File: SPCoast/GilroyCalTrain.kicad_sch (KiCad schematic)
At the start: 90 parts, among them SW3771 771, SW3773 773, SW3775 775

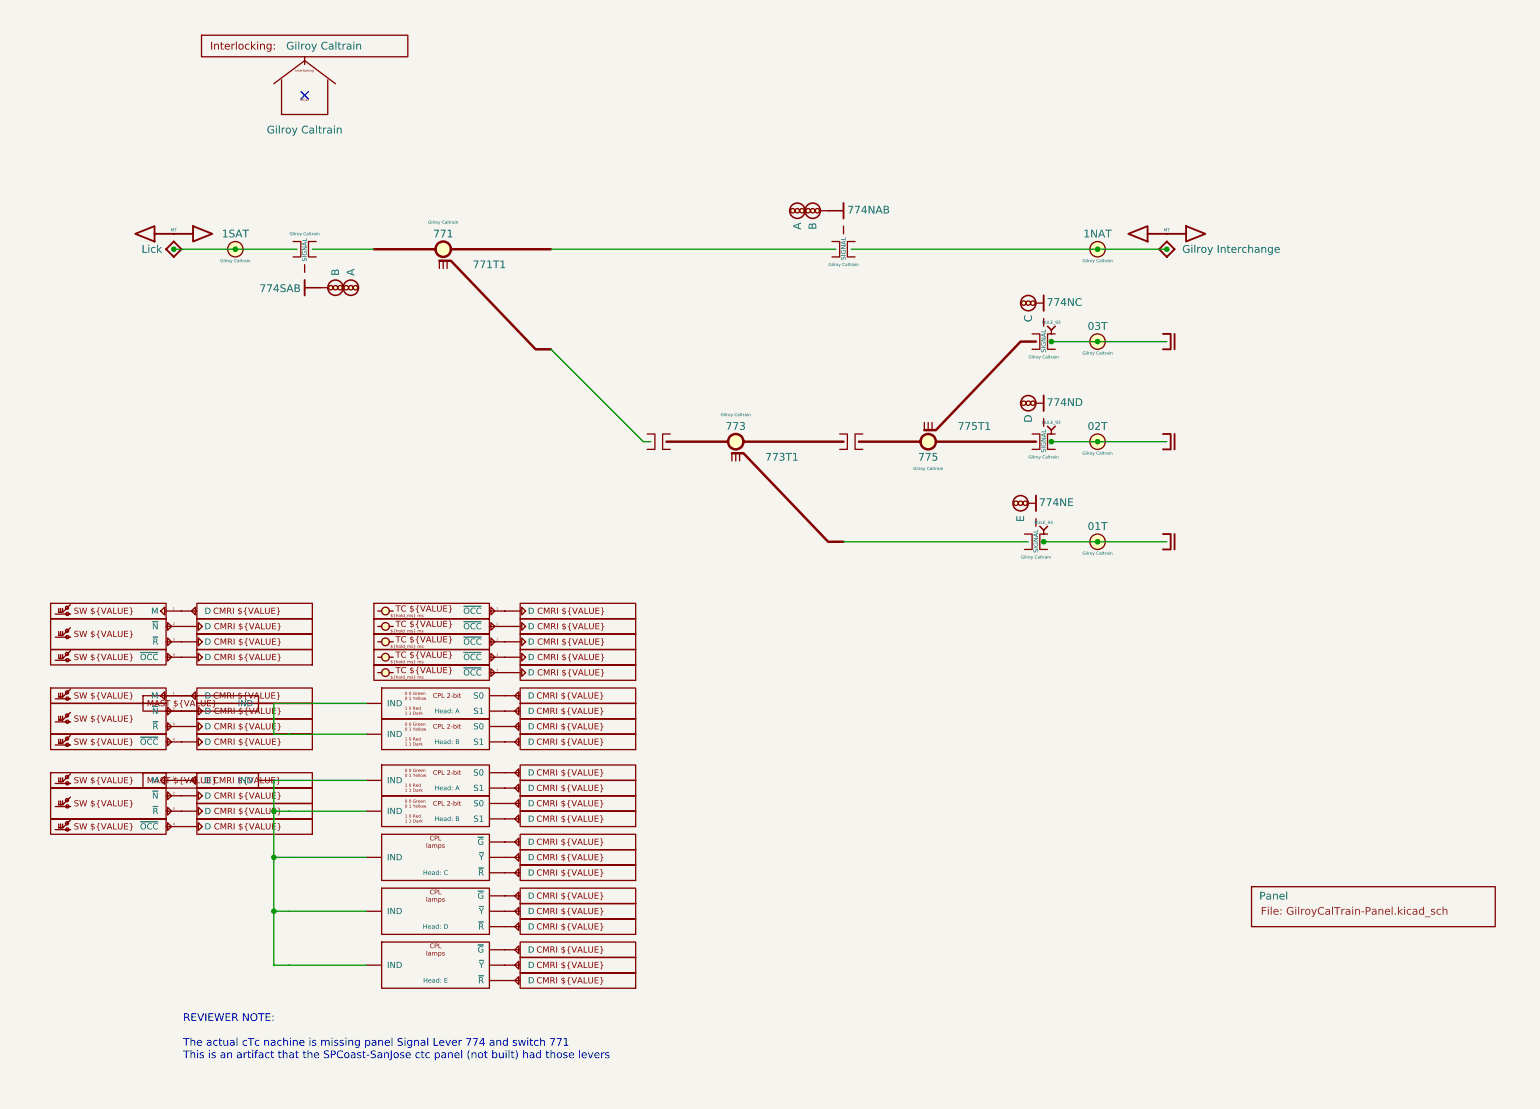
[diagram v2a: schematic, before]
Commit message: refactor(kicad): one Mast per trackplan mast; no library defaults for per-instance facts
Owner's regroup (Sargent, Gilroy Caltrain): the Mast anchors are now the
trackplan masts, Value for Value: 836NAB, 836SA, 836SB, 774NAB, 774SAB,
774NC, 774ND, 774NE. Each head cast hangs on the IND of the mast whose name
lists its letter; 836SB carries its semaphore arm and spectacle RGB as one
Head B. The earlier "836S"/"774N" masts were a lever-direction grouping,
not masts, and are gone. Sargent Exp2 (PCA9685 0x27) channels re-placed by
the owner; the two stray IND stubs on Caltrain removed.

Owner's library tidy: cast bodies one width (-21.59..-2.54), IND pin at
-24.13, Head shown 1.27 left-justified, encoder table outside the body,
Semaphore Style hidden behind "${STYLE} arm".

Library defaults that are per-instance facts are now empty, so KiCad's
field reset can no longer plant plausible wrong values: PanelLamp-*
IndicationToken (was "S"), PanelColumn Interlocking (was "Luchessa"),
Codeline-Encoding-*/Transport-MQTT Station (was "${SHEETNAME}", which
resolves to "Panel"), Interlocking Value (was "${TITLE}"), MCP23017 and
PCA9685 Address (was "0x20"). Mast and Cast-Head-* descriptions follow the
model: Value = the trackplan mast; Head = one of the letters its name lists.

The owner's save had run "Update Symbols from Library" with field reset a
second time; 94 per-instance values (IndicationToken, Interlocking,
Station, Exp2 0x27) restored from the last good netlist by
edits/2026-10-17-restore-reset-fields.py. Its stale CMRI entries wrote bit
numbers into 32 Caltrain CMRI Addresses on the way; put back to 30 and the
entries removed. Sheet lib_symbols caches refreshed (45) to the libraries.

Verified:
- kicad-cli ERC, all severities: 0 violations
- lint_symbol_fields.py: 90 symbols, 0 errors
- sync-library-fields dry run: 0 instances to change
- production/post-head.net vs production/post-restore.net: every mast Value
  is a trackplan mast on its sheet; every cast sits on on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
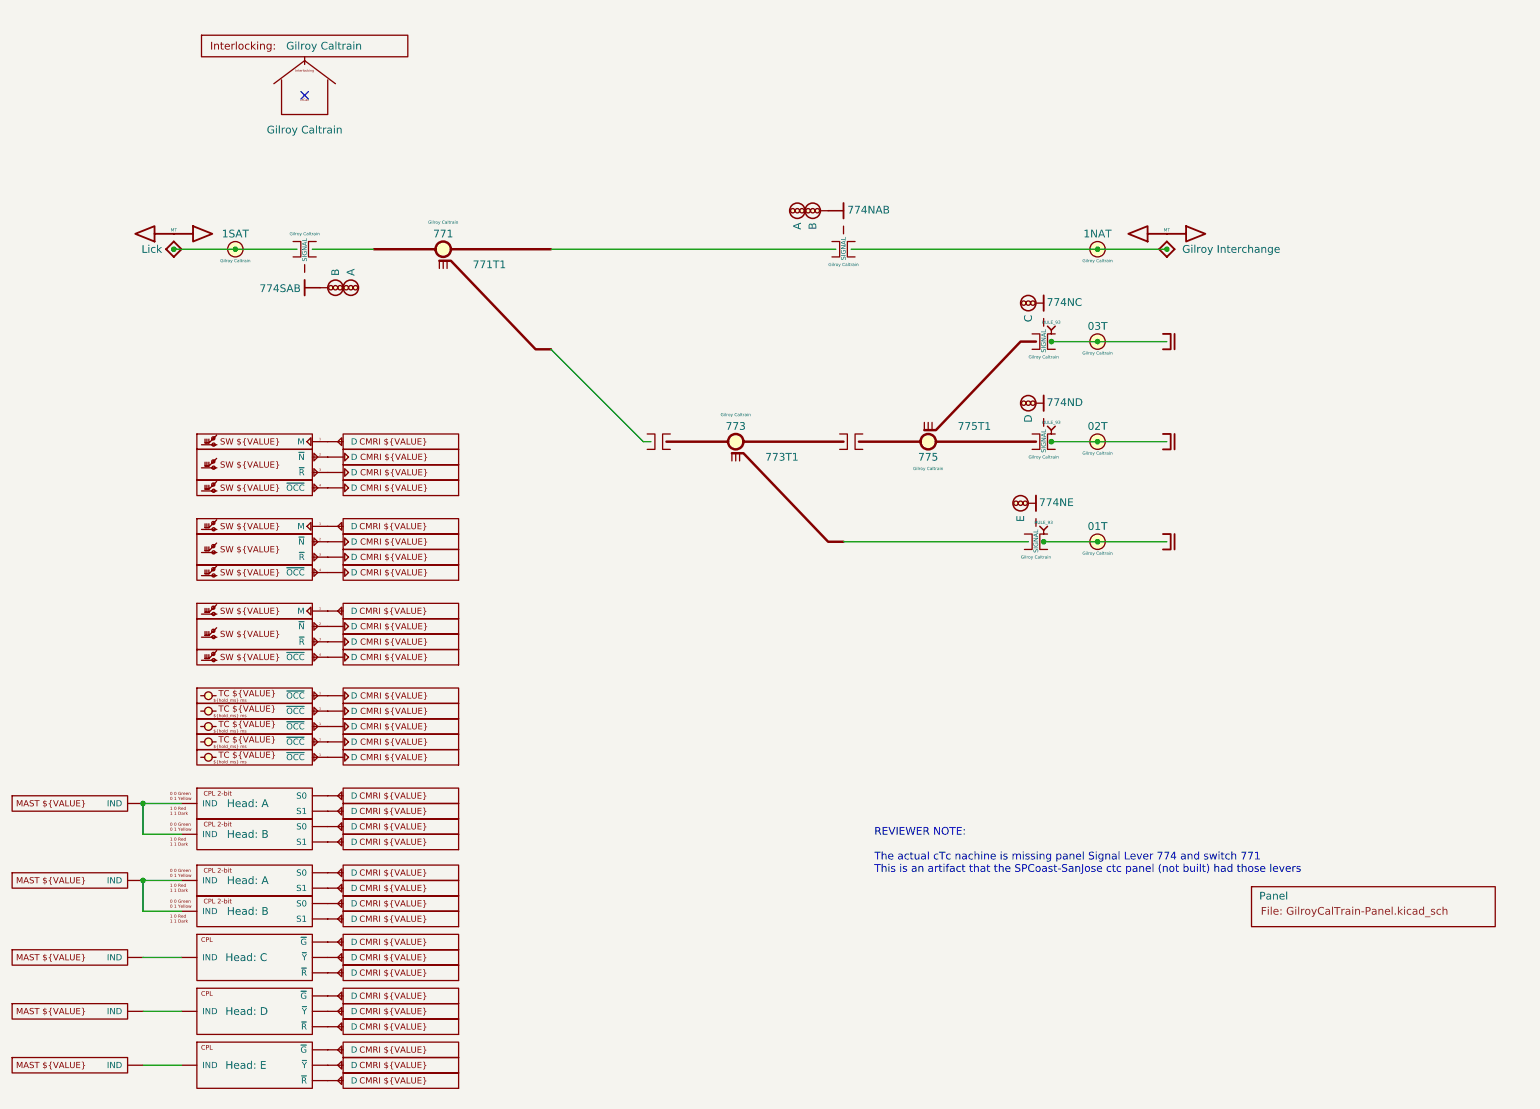
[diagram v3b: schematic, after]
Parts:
- added DevMast5: 774NC, symbol Railroad-Field:Mast
- added DevMast6: 774ND, symbol Railroad-Field:Mast
- added DevMast7: 774NE, symbol Railroad-Field:Mast
- DevMast3: value 774N -> 774NAB
- DevMast4: value 774S -> 774SAB
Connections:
- net at Cast11.3 (IND), Cast8.3 (IND), DevMast3.1 (IND): no longer Cast6.4 (IND), Cast7.4 (IND), Cast9.4 (IND)
- new net: Cast9.4 (IND), DevMast7.1 (IND)
- new net: Cast6.4 (IND), DevMast6.1 (IND)
- new net: Cast7.4 (IND), DevMast5.1 (IND)

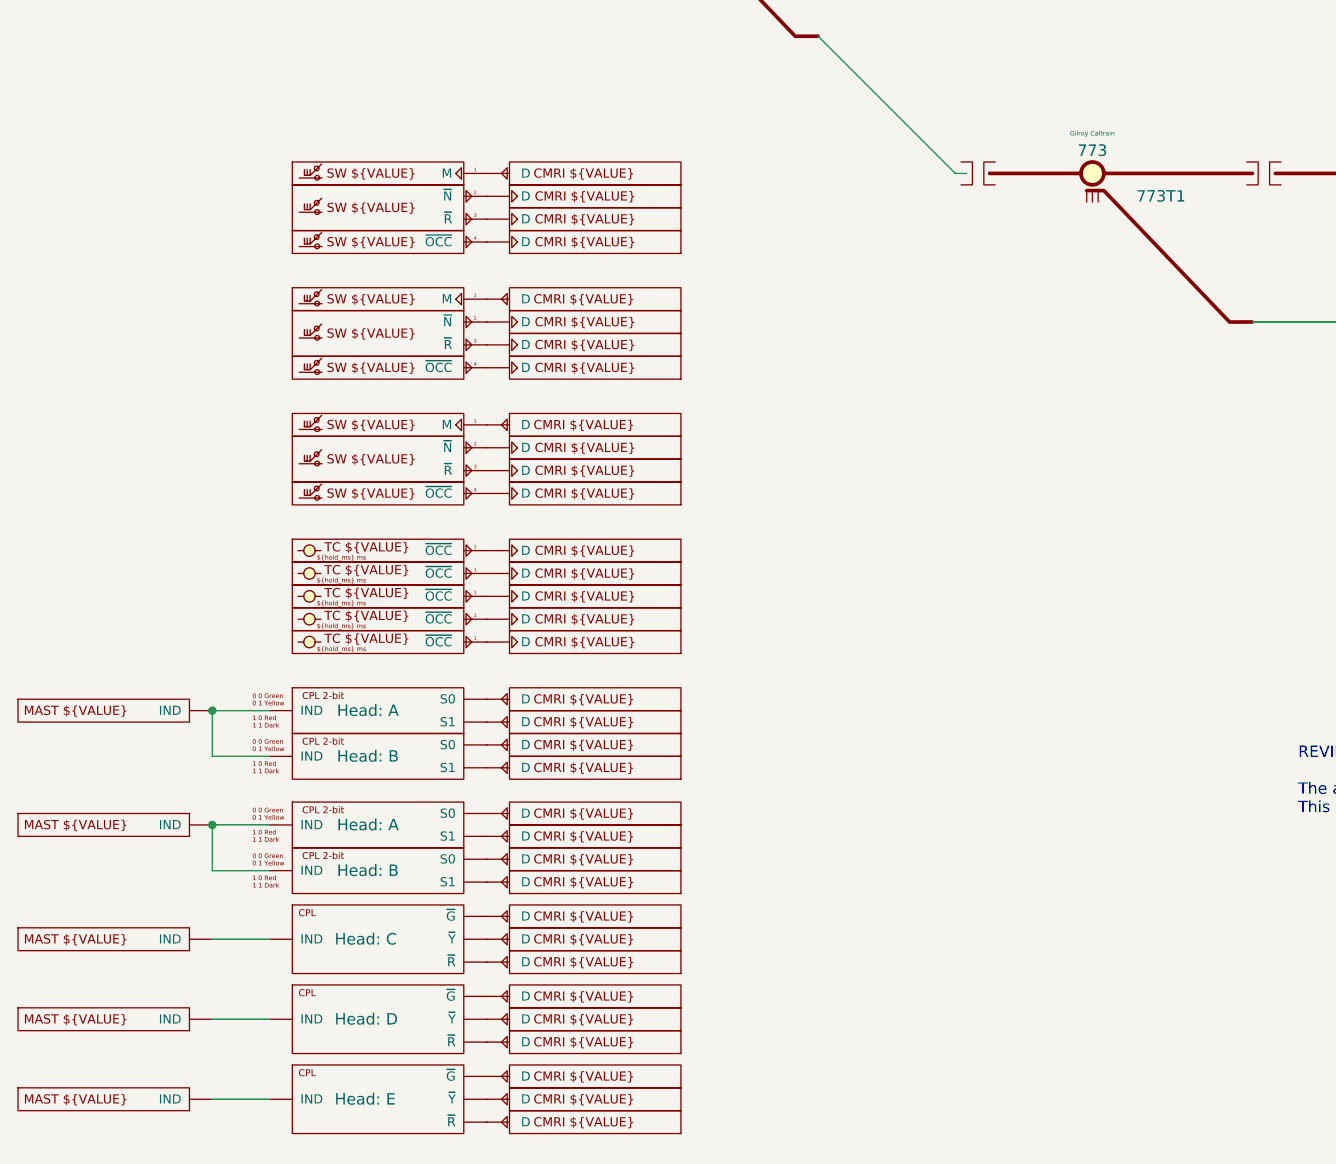
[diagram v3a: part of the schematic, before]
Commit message: chore(kicad): owner edits: GPIO drivers carry Address, Sargent I2C addresses, CMRI body text from fields
Baseline of the owner's saved work before the ADR 0005 scripts:
- Driver-GPIO-Digital and Driver-GPIO-Pixel gain an Address field (the
  board pin); Value renders ${Address}; body text and arrow adjusted.
- Driver-CMRI-IB/OB body text renders UA${Address}.IN/OUT.${Bit} from
  the fields instead of ${VALUE}.
- Sargent, Gilroy Interchange and Luchessa GPIO instances carry Address;
  Sargent Exp2 back at 0x26, Exp3 0x27.
- All sheets resaved by KiCad 10 (reordering), project file
  used_designators cleared by KiCad.

Verified: no lock files; committed as saved, unverified by netlist (the
baseline netlist is exported in the next step).

Co-Authored-By: Claude Fable 5.1 <noreply@anthropic.com>
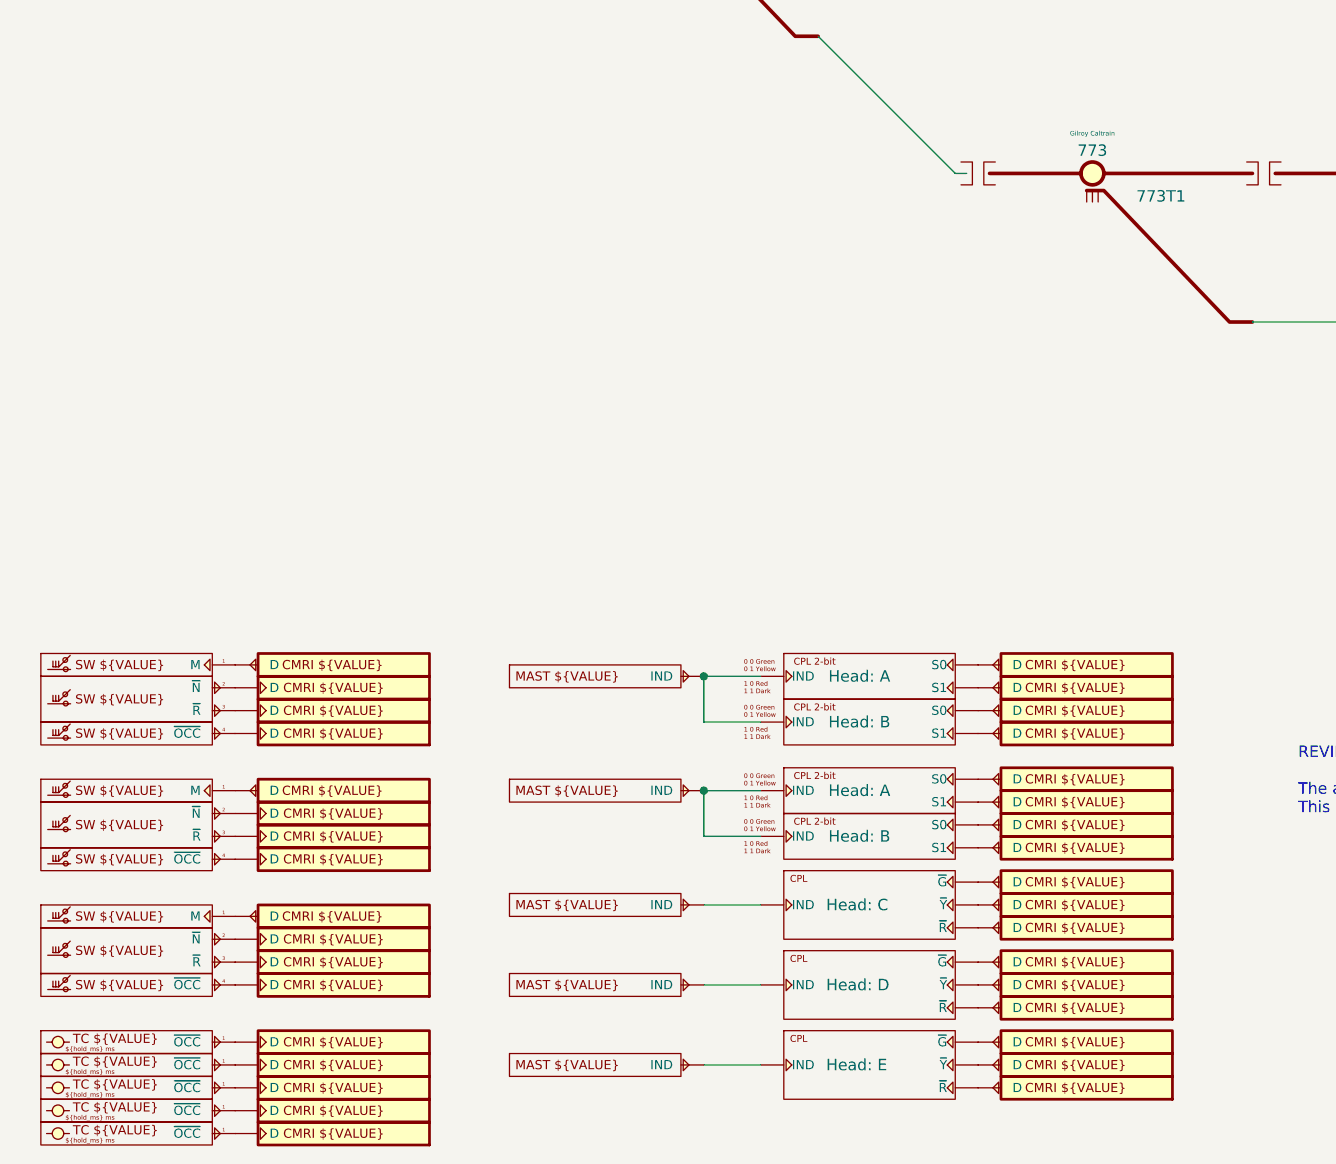
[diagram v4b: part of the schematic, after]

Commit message: feat(kicad): Processor declares the Caltrain CMRInet node; drivers carry Bit only (ADR 0005)
ADR 0005 §9 applied by SPCoast/edits/2026-10-19-processor-node.py:
- Railroad-HardwareIO: new Processor symbol (Role STRUCTURE, Kind
  PROCESSOR, no pins; Board, Transport, Address); Driver-CMRI-IB/OB lose
  UA and Address, Value renders IN.${Bit} / OUT.${Bit}, body text and
  Description follow.
- Railroad-Office: every Codeline-Transport-* gains Host (empty = the
  office processor).
- Gilroy Caltrain: one Processor "Caltrain" (Transport CMRInet, Address
  30, Board cpNode) placed right of the Interlocking box; the 34 CMRI
  drivers lose UA and Address (68 field values); embedded definitions of
  the three symbols refreshed.
- South-cTc: the MQTT transport loses Station (an encoding fact, ADR
  0001); the four transports gain Host ""; their embedded definitions
  refreshed.

Verified: gate script 2026-10-19-processor-node-gate.py PASS on
production/pre-processor.net vs post-processor.net exported from
SPCoast.kicad_sch (716 nets unchanged, 586 -> 587 parts, exactly the
expected field delta, no other field change, ERC zero before and after);
its --self-test shows the gate fails on a leftover UA, a dropped net and
an unrelated field change. KiCad's forced resave on copies is
byte-identical for both libraries and South-cTc; GilroyCalTrain was
adopted from that resave after checking only the new block's position
differed. Subdivision Role lint: 91 symbols, 0 errors; kicad-cli sym
export svg of Processor and the sheet checked by eye. No lock files;
KiCad closed by the owner.

Co-Authored-By: Claude Fable 5.1 <noreply@anthropic.com>
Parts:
- added Proc1: Caltrain, symbol Railroad-HardwareIO:Processor
- CMRI1, CMRI18, CMRI19, CMRI20, CMRI21, CMRI22, CMRI23, CMRI24, CMRI25, CMRI26, CMRI27, CMRI28, CMRI29, CMRI30, CMRI31, CMRI32, CMRI33, CMRI34, CMRI5, CMRI9: value UA${Address}.OUT.${Bit} -> OUT.${Bit}; Address 30 -> (none); UA ${Address} -> (none)
- CMRI10, CMRI11, CMRI12, CMRI13, CMRI14, CMRI15, CMRI16, CMRI17, CMRI2, CMRI3, CMRI4, CMRI6, CMRI7, CMRI8: value UA${Address}.IN.${Bit} -> IN.${Bit}; Address 30 -> (none); UA ${Address} -> (none)
